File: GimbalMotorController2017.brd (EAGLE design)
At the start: 112.4 x 80 mm, 124 parts, among them J3 APP_2POS_CONFIG5V_HORIZ, Q7 MOSFET-PCHANNEL, Q8 MOSFET-PCHANNEL, Q9 MOSFET-NCHANNELAO3404A, U1 NUP4201MR6, U2 MAX3232D, U3 CSD18533Q5A, U4 CSD18533Q5A, U5 CSD18533Q5A, U6 CSD18533Q5A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

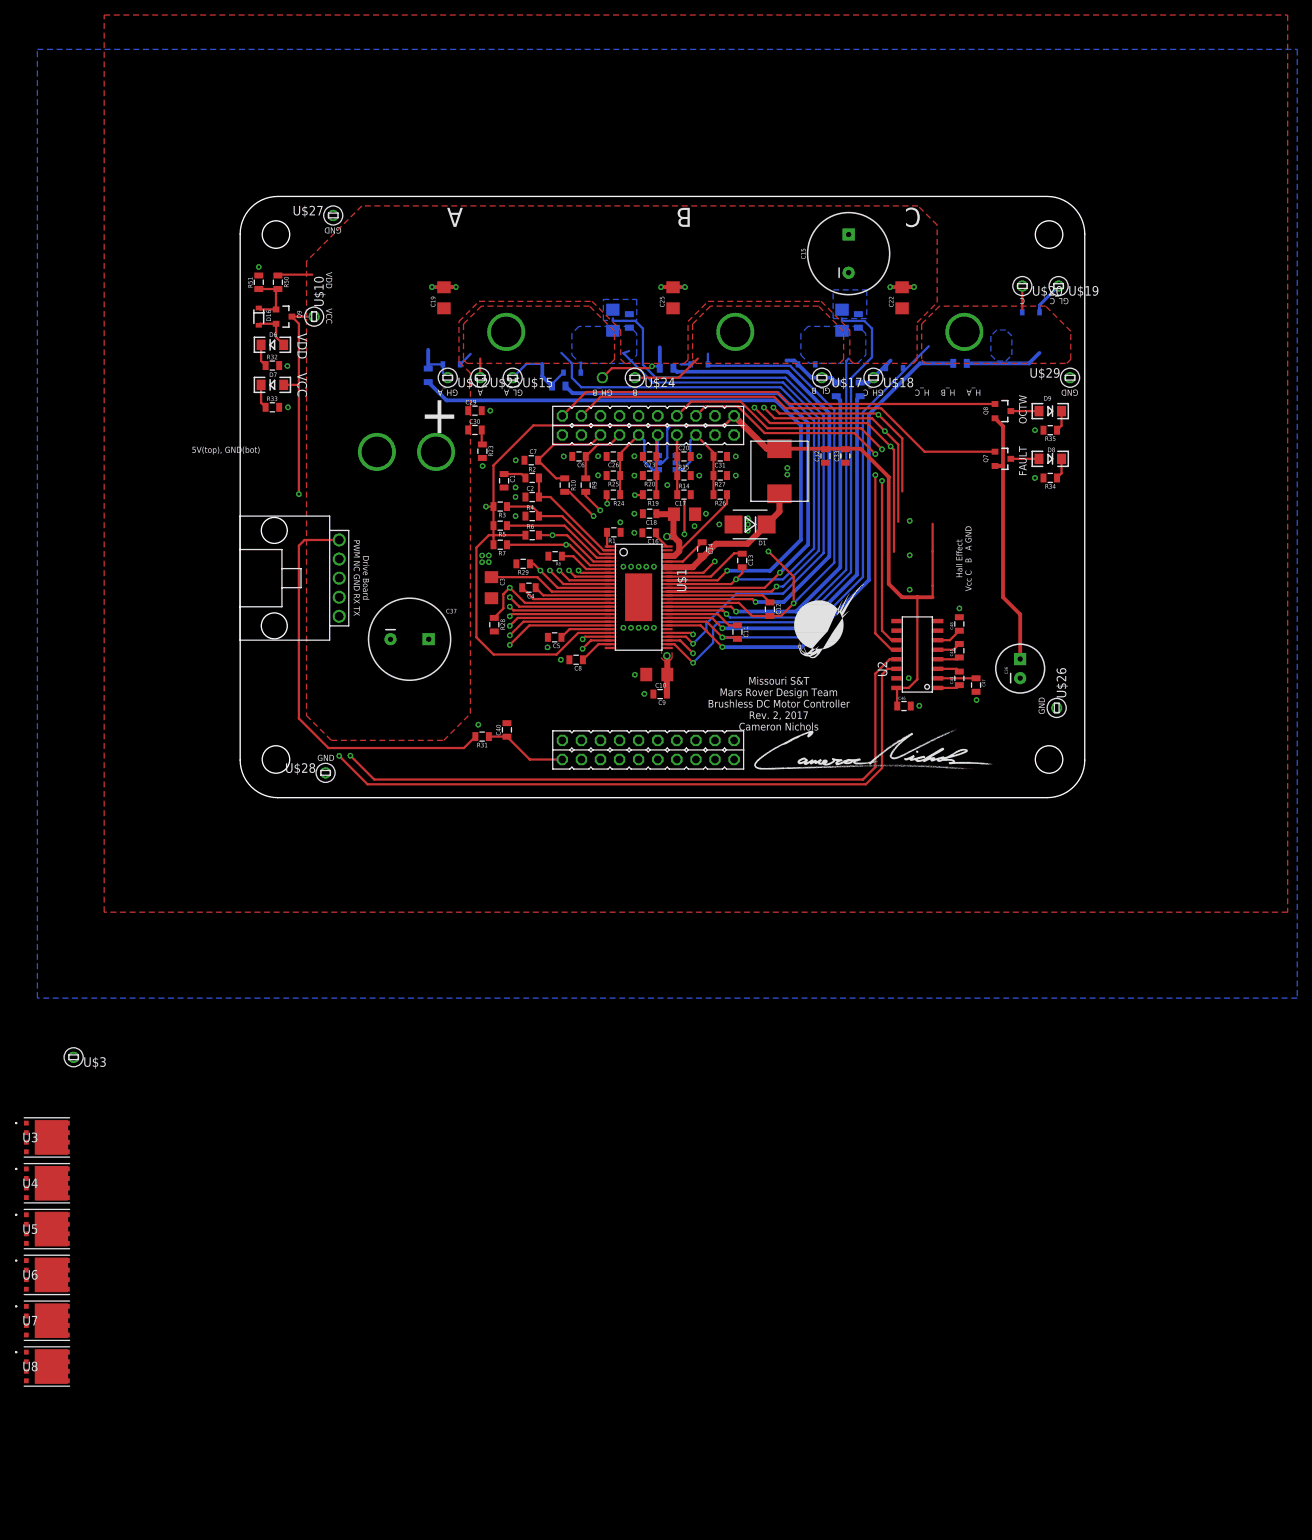
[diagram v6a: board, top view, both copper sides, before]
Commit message: Shrank size to roughly 11 square inches, moved lots of components and ripped up wires
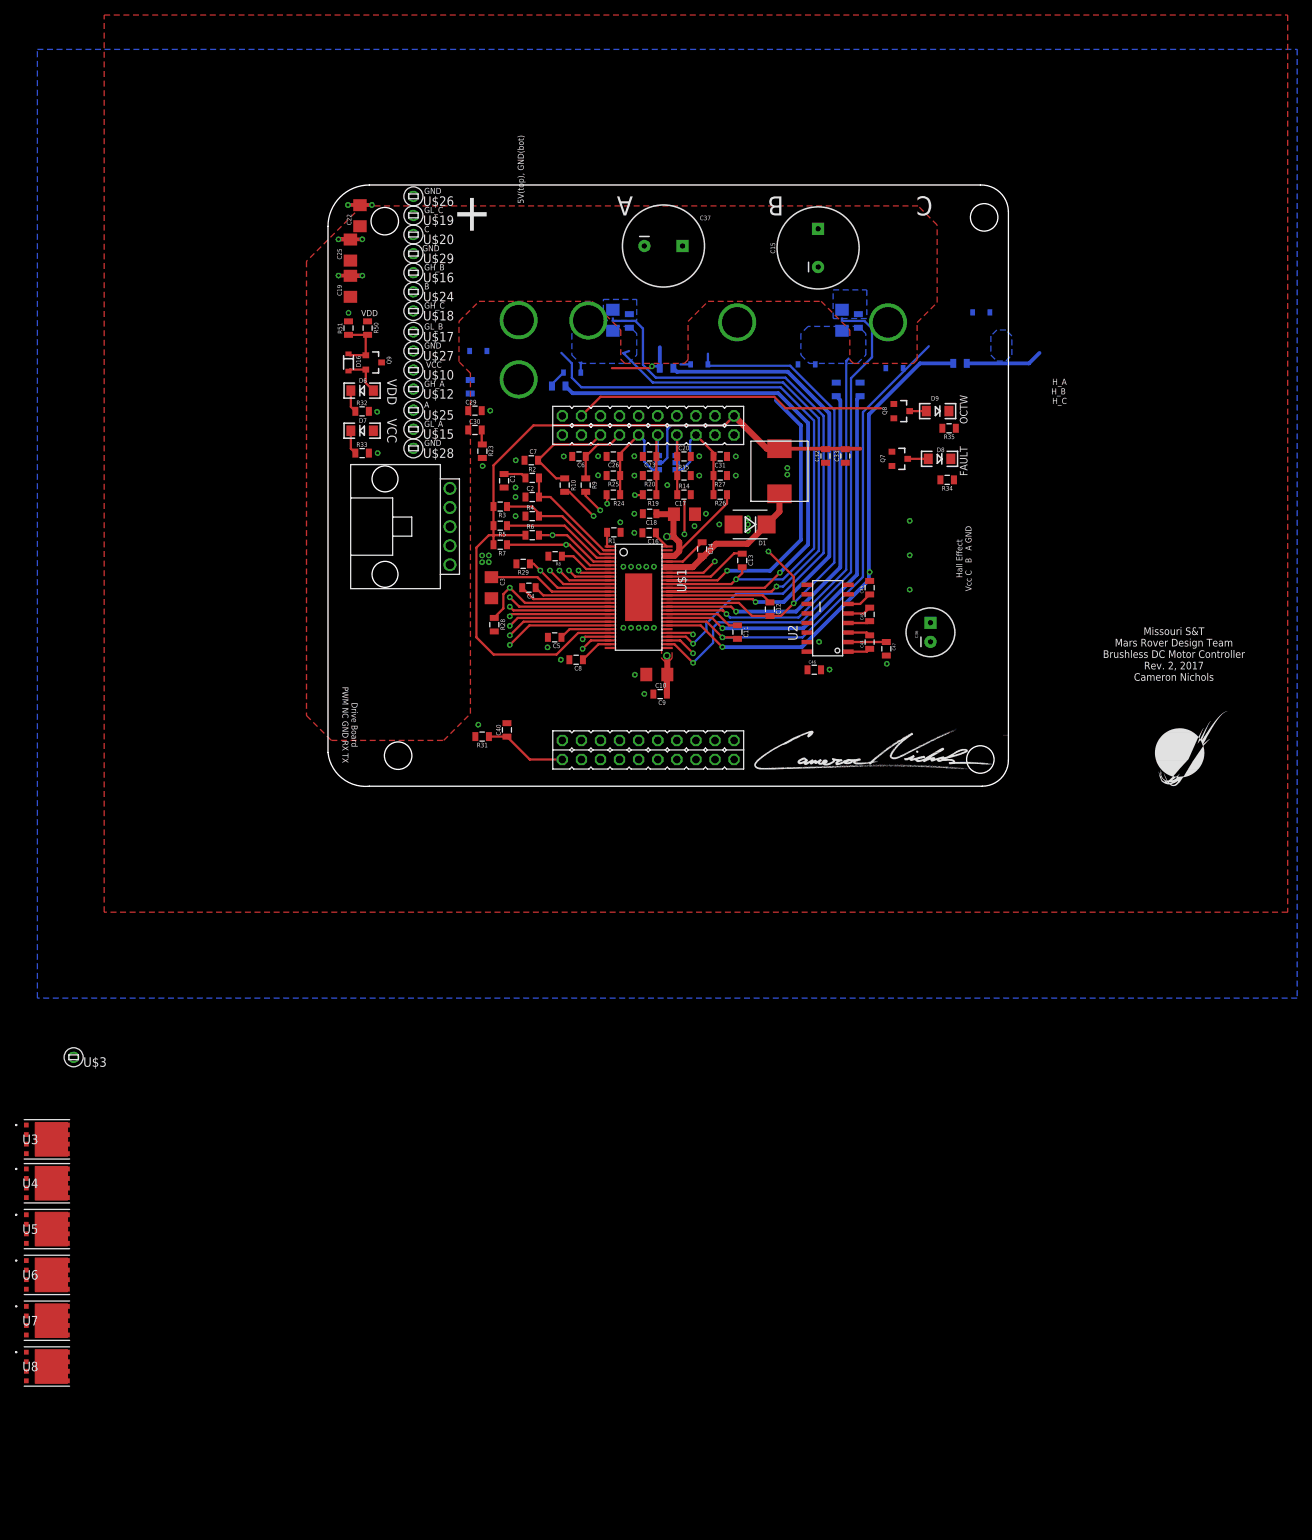
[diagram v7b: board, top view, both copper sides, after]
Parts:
- moved U$26 109.4 mm to (20.8, 78.7), turned to 0 degrees
- moved U$29 88.9 mm to (20.8, 71.1), turned to 0 degrees
- moved U$19 86.4 mm to (20.8, 76.2)
- moved U$20 81.3 mm to (20.8, 73.7)
- moved C22 73.0 mm to (13.7, 76.2)
- moved J3 65.8 mm to (30.9, 90.5), turned to 270 degrees
- moved C37 62.3 mm to (54.1, 72.1)
- moved U$18 61.9 mm to (20.8, 63.5)
- moved U$17 54.7 mm to (20.8, 60.7)
- moved U$9 50.9 mm to (119.5, -0.58)
- moved U$28 44.7 mm to (20.8, 45.2), turned to 0 degrees
- moved C25 43.4 mm to (12.4, 71.6)
- moved U$24 31.6 mm to (20.8, 66.0)
- moved U$16 28.8 mm to (20.8, 68.6), flipped to the top
- moved U$27 21.0 mm to (20.8, 58.2), turned to 0 degrees
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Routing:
- net VCC: track 297.2 -> 154.7 mm, vias 3 -> 1
- net 232_RX: track 109.7 -> 0.00 mm, vias 1 -> 0
- net 232_TX: track 108.0 -> 0.00 mm, vias 1 -> 0
- net NOCTW: track 86.9 -> 27.4 mm
- net HALL_B: track 58.6 -> 0.00 mm, vias 2 -> 0
- net HALL_A: track 57.5 -> 0.00 mm, vias 2 -> 0
- net UART_TX: track 57.4 -> 0.00 mm, vias 2 -> 0
- net UART_RX: track 54.7 -> 0.00 mm, vias 2 -> 0
- net HALL_C: track 54.6 -> 0.00 mm, vias 2 -> 0
- net N$34: track 54.4 -> 0.00 mm
- net GH_A: track 89.7 -> 42.4 mm
- net NFAULT: track 92.0 -> 74.4 mm
- net SH_B: track 106.8 -> 97.4 mm
- net N$16: track 10.6 -> 2.43 mm
- net N$15: track 7.85 -> 0.00 mm
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- removed copper zone on layer 1, net SH_A
- removed copper zone on layer 1, net SH_B
- removed copper zone on layer 1, net SH_C
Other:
- board size 112.4 x 80 mm -> 90.5 x 80 mm

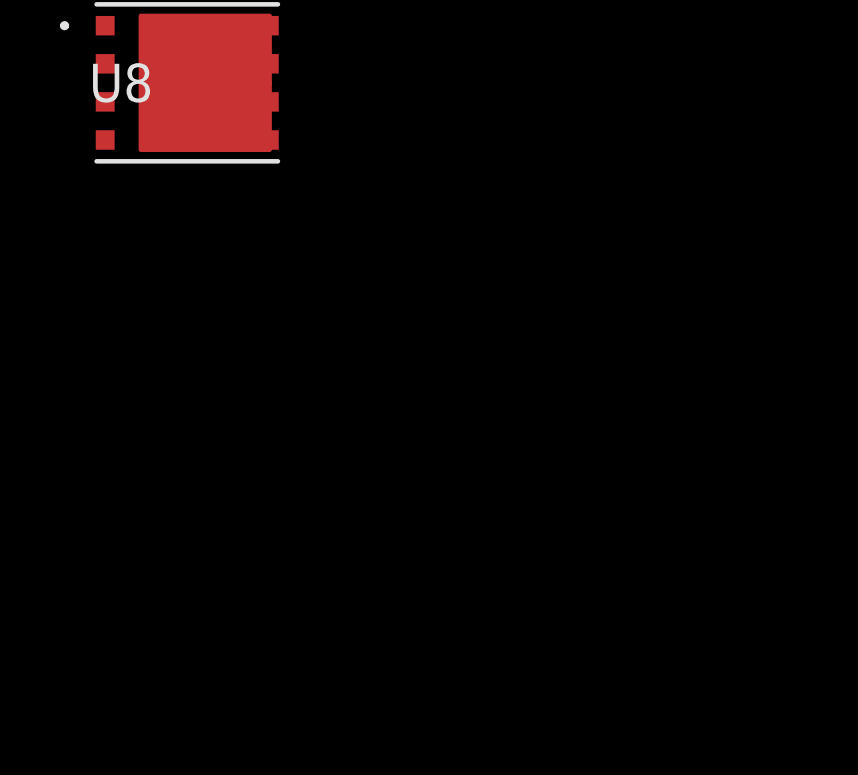
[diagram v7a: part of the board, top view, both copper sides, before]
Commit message: Add pwm connector to external connections
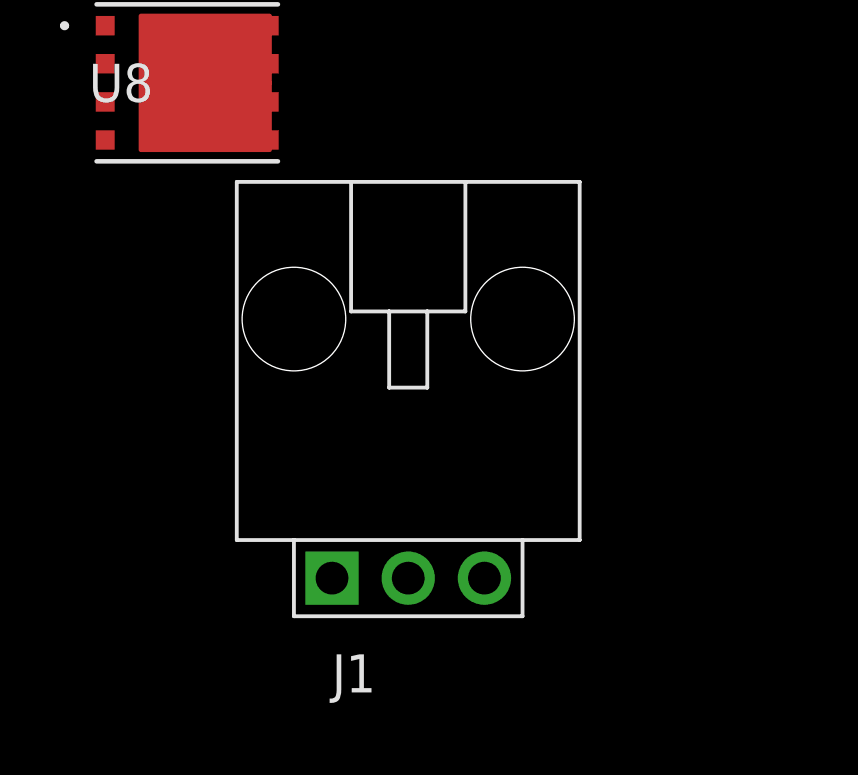
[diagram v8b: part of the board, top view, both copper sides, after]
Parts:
- added J1: SL03THROUGH_HOLE, MRDT-Connectors:MOLEX_SL_03_TH
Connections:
- new net PWM_IN_NO_FILTER: J1.3, U$2.PF4
- net GND: now also J1.1
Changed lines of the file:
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@@
 <attribute name="VENDOR" value="Texas Instruments" x="-27.94" y="-76.962" size="1.778" layer="27" display="off"/>
+</element>
+<element name="J1" library="MRDT-Connectors" package="MOLEX_SL_03_TH" value="SL03THROUGH_HOLE" x="-20.574" y="-93.472">
+<attribute name="ORIENT" value="HORIZ" x="-20.574" y="-93.472" size="1.778" layer="27" display="off"/>
+<attribute name="PARTNO" value="0705550002" x="-20.574" y="-93.472" size="1.778" layer="27" display="off"/>
 </element>
 </elements>
@@
 <wire x1="15.3035" y1="77.597" x2="13.74475" y2="77.597" width="0.508" layer="1"/>
 <wire x1="13.74475" y1="77.597" x2="13.716" y2="77.56825" width="0.4064" layer="1"/>
+<contactref element="J1" pad="1"/>
 <wire x1="80.04175" y1="63.0665" x2="95.243" y2="63.3095" width="0" layer="19" extent="16-16"/>
 <wire x1="77.851" y1="63.66175" x2="80.04175" y2="63.0665" width="0" layer="19" extent="16-16"/>
@@
 <wire x1="63.5" y1="3.81" x2="52.7575" y2="12.5095" width="0" layer="19" extent="1-1"/>
 <wire x1="-30.675071875" y1="-53.213" x2="29.464" y2="8.4455" width="0" layer="19" extent="1-1"/>
+<wire x1="-23.114" y1="-93.472" x2="-30.675071875" y2="-53.213" width="0" layer="19" extent="1-1"/>
 </signal>
 <signal name="N$3">
@@
 <contactref element="U$3" pad="P$1"/>
 </signal>
+<signal name="PWM_IN_NO_FILTER">
+<contactref element="J1" pad="3"/>
+<contactref element="U$2" pad="PF4"/>
+<wire x1="40.64" y1="6.35" x2="-18.034" y2="-93.472" width="0" layer="19" extent="1-1"/>
+</signal>
 </signals>
